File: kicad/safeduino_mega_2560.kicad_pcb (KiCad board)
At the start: 4 copper layers, 134.5 x 63.9 mm, 104 parts, among them X1 USBB-1J

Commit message: Закончил предварительную трассировку платы.
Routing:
- net /PA6: track 62.0 -> 72.1 mm, vias 2 -> 3
- net /PA1: track 74.7 -> 64.7 mm
- net /PA0: track 78.5 -> 70.3 mm
- net /PA4: track 68.1 -> 76.0 mm, vias 2 -> 3
- net /SCK: track 50.9 -> 57.8 mm
- net /PJ3: track 44.1 -> 50.8 mm
- net /SS: track 53.7 -> 60.1 mm
- net /PD0: track 55.0 -> 49.8 mm
- net /MISO: track 52.6 -> 57.5 mm
- net /VCCIN: track 92.2 -> 88.8 mm, vias 0 -> 1
- net /PD2: track 49.4 -> 46.1 mm
- net /PE6: track 77.6 -> 74.8 mm
- net /MPU_VCC: track 392.4 -> 389.6 mm, vias 9 -> 8
- net /RESET: track 87.5 -> 90.2 mm
- net /PL7: track 37.4 -> 34.8 mm
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
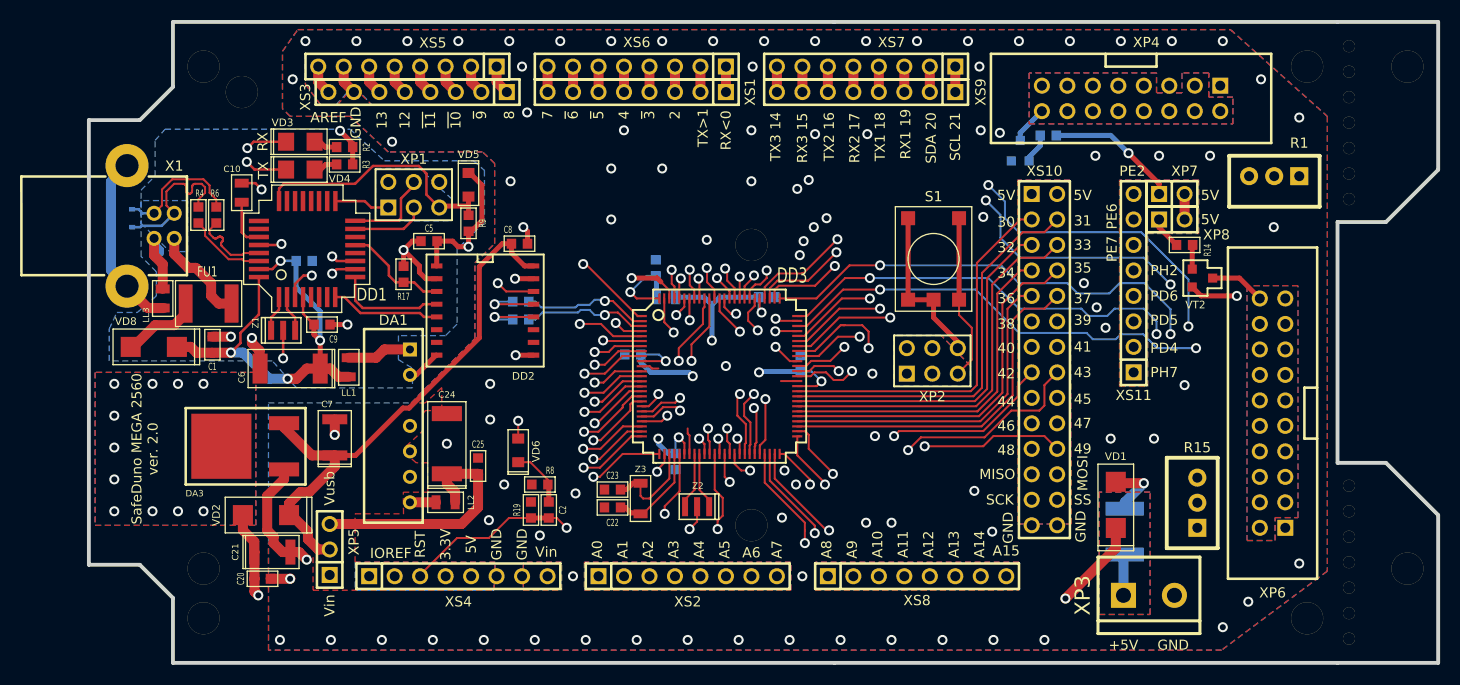
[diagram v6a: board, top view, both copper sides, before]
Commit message: Добавил в схему различные варианты подключения резистора регулировки контрастности для графического дисплея.
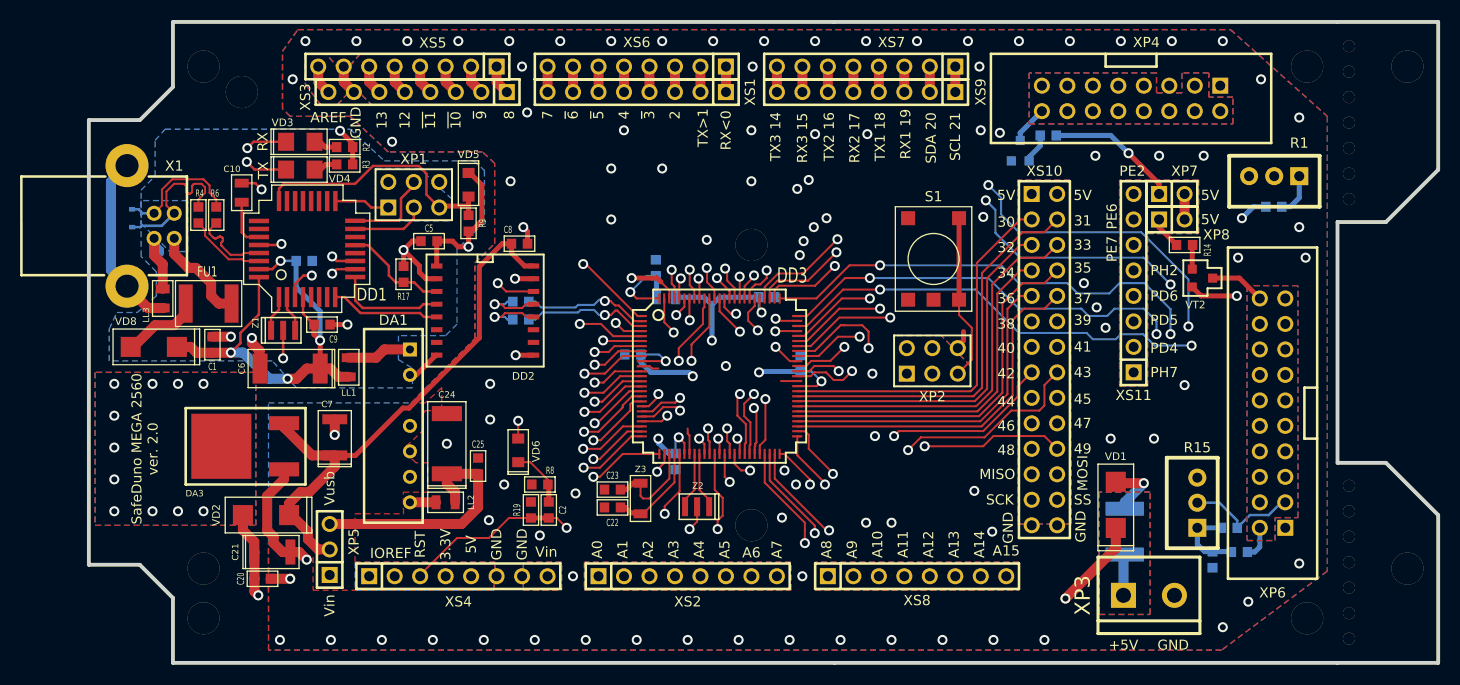
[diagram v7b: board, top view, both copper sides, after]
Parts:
- added R10: 0, IWsmd_case:SMD0603, B.Cu at (164.1, 143.1)
- added R13: 0, IWsmd_case:SMD0603, B.Cu at (165.7, 140.0)
- added R16: 0, IWsmd_case:SMD0603, B.Cu at (170.2, 108.0)
- added R7: 0, IWsmd_case:SMD0603, B.Cu at (166.8, 142.4)
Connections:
- R1 pad 1: /MPU_VCC -> Net-(R1-Pad1)
- R15 pad 1: /MPU_VCC -> Net-(R10-Pad2)
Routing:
- net /GND: track 61.8 -> 47.2 mm, vias 90 -> 92
- net Net-(R10-Pad2): track 0.00 -> 7.73 mm
- net Net-(R1-Pad1): track 0.00 -> 4.14 mm
- net /MPU_VCC: track 389.6 -> 387.2 mm, vias 8 -> 9
- net /VO_LCD: track 10.7 -> 12.6 mm
- net /PH1: track 56.1 -> 55.2 mm
- net /PJ5: track 45.6 -> 44.9 mm
- net /PH0: track 53.0 -> 52.4 mm
- net /PJ1: track 37.5 -> 38.0 mm

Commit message: Сохранил проект печатной платы в KiCad 6.0.2. и исправил недочёты в трассировке.
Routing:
- net /ADC9: track 37.7 -> 33.6 mm
- net /MPU_VCC: track 387.2 -> 383.2 mm
- net /VO_LCD: track 12.6 -> 10.9 mm
- net /GND_USB: track 38.4 -> 36.9 mm
- net /PJ5: track 44.9 -> 43.8 mm
- net /PE7: track 78.9 -> 77.8 mm
- net Net-(R1-Pad2): track 13.5 -> 12.5 mm
- net /5V_USB: track 117.8 -> 116.9 mm
- net /PE6: track 74.8 -> 73.8 mm
- net /PB5: track 56.5 -> 55.7 mm
- net /PD0: track 49.8 -> 49.2 mm
- net /PC3: track 63.1 -> 62.6 mm
- net /PC1: track 69.0 -> 68.4 mm
- net /PH4: track 45.1 -> 44.6 mm
- net /V_OUT: track 19.1 -> 18.6 mm
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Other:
- net class Default removed
- board text added: "~{10}"
- board text added: "~{11}"
- board text added: "~{3}"
- board text added: "~{5}"
- board text added: "~{6}"
- board text added: "~{9}"
- board text removed: "~10"
- board text removed: "~11"
- board text removed: "~3"
- board text removed: "~5"
- board text removed: "~6"
- board text removed: "~9"
